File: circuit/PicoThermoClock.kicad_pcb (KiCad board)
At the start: 4 copper layers, 100 x 100 mm, 41 parts, among them J1 USB_B_Micro, J2 AVR-ISP-6, J3 Conn_01x03, J4 Conn_01x03, Q1 SS9012H, Q2 SS9012H, Q3 SS9012H, Q4 SS9012H, Q5 C1815GR, SW1 SW_Push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

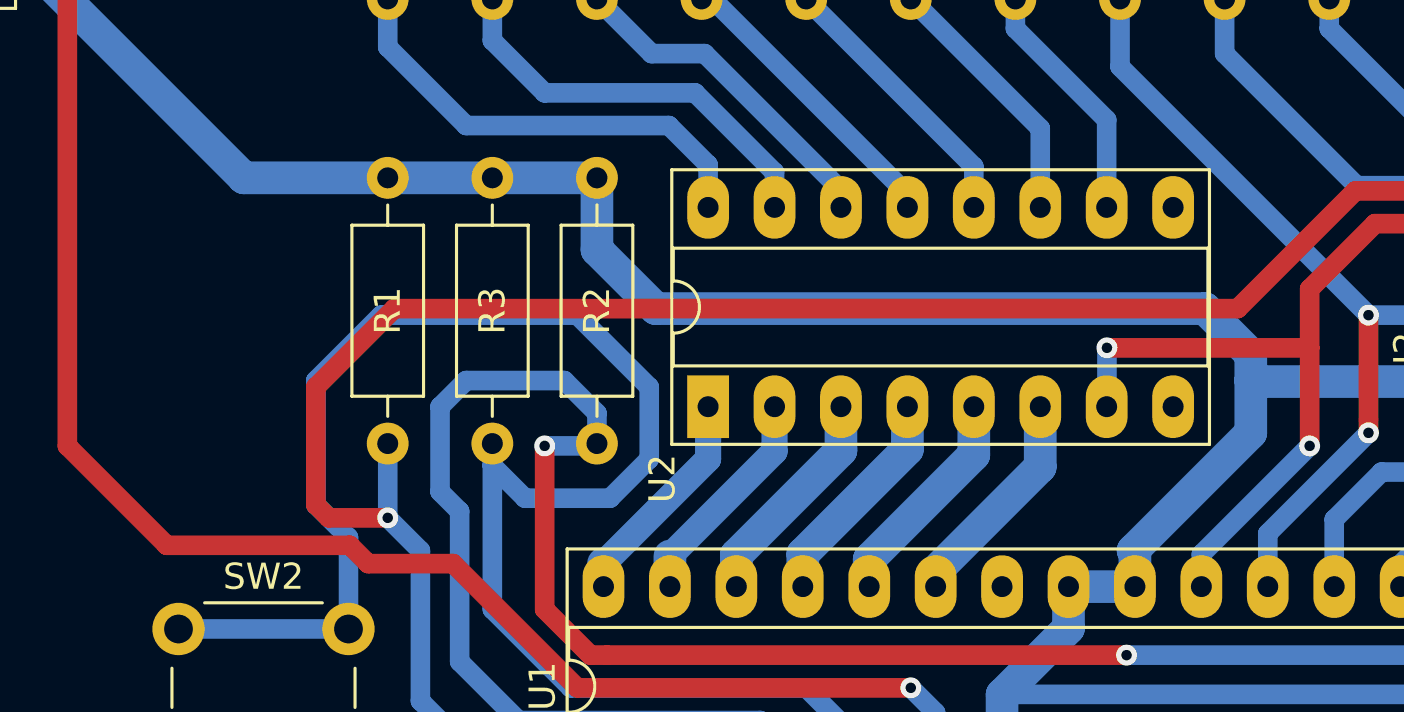
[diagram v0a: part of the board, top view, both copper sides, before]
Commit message: Fix missing resistor
Add additional path widths
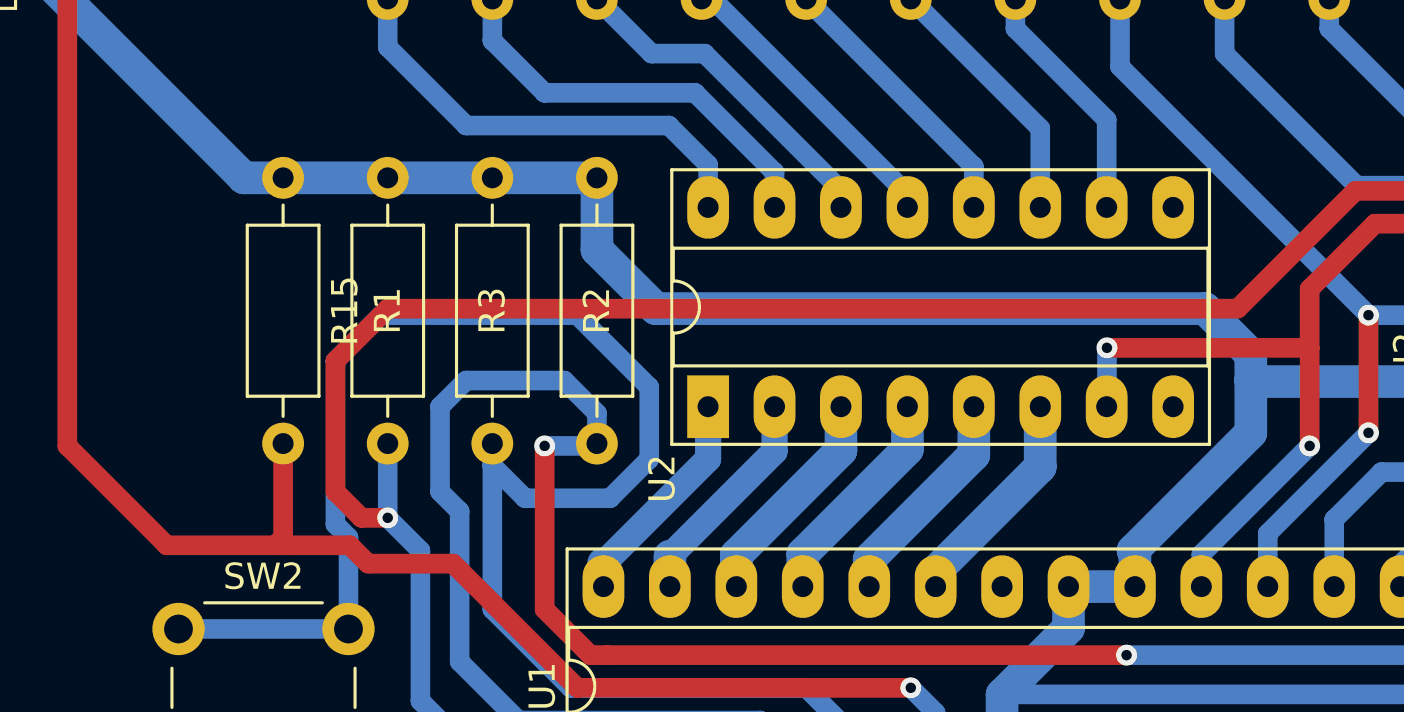
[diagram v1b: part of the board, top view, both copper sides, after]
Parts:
- added R15: 4k7, Resistor_THT:R_Axial_DIN0207_L6.3mm_D2.5mm_P10.16mm_Horizontal, F.Cu at (117.5, 83.2)
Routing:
- net Net-(J4-Pad2): track 89.2 -> 93.2 mm
- net RST: track 82.8 -> 81.6 mm
- net Net-(R3-Pad2): track 65.7 -> 65.0 mm
